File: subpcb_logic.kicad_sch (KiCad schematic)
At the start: 64 parts, among them J1 Conn_01x04, J12 xcore, J13 Screw_Terminal_01x02, J14 Conn_01x02, J15 Conn_01x04, J16 67800-8005, J18 67800-8005, J24 Conn_01x02, J25 67800-8005, J26 67800-8005, J27 67800-8005, J28 Conn_01x03_Male, J30 Conn_01x03_Male, J31 Conn_01x03_Pin, J52 Conn_01x03_Male, J54 Conn_01x03_Male, M1 Fan, Q1 AO3400A, Q2 AO3400A, U5 M24C02-WMN, U6 AS-RTK2B-MICRO-F9P-L1L2SMATH-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, U7 TXS0108EPW

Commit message: Added JLC part for xCore connector
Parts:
- J12: JLC (none) -> C306045
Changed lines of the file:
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@@
 			)
 		)
+		(property "JLC" "C306045"
+			(at 365.76 370.84 0)
+			(effects
+				(font
+					(size 1.27 1.27)
+				)
+				(hide yes)
+			)
+		)
 		(pin "114"
 		)
@@
 			)
 		)
+		(property "JLC" "C306045"
+			(at 201.93 424.18 0)
+			(effects
+				(font
+					(size 1.27 1.27)
+				)
+				(hide yes)
+			)
+		)
 		(pin "114"
 		)
@@
 			)
 		)
+		(property "JLC" "C306045"
+			(at 96.52 436.88 0)
+			(effects
+				(font
+					(size 1.27 1.27)
+				)
+				(hide yes)
+			)
+		)
 		(pin "114"
 		)
@@
 			)
 		)
+		(property "JLC" "C306045"
+			(at 97.79 345.44 0)
+			(effects
+				(font
+					(size 1.27 1.27)
+				)
+				(hide yes)
+			)
+		)
 		(pin "114"
 		)
@@
 			(at 364.49 425.45 0)
 			(effects
+				(font
+					(size 1.27 1.27)
+				)
+				(hide yes)
+			)
+		)
+		(property "JLC" "C306045"
+			(at 364.49 425.45 0)
+			(effects

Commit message: Updated to the non-pcb mount xt30 connectors
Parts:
- J14: footprint Connector_AMASS:AMASS_XT30UPB-M_1x02_P5.0mm_Vertical -> Connector_AMASS:AMASS_XT30U-M_1x02_P5.0mm_Vertical; JLC C428721 -> C99101
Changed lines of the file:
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@@
 			)
 		)
-		(property "Footprint" "Connector_AMASS:AMASS_XT30UPB-M_1x02_P5.0mm_Vertical"
+		(property "Footprint" "Connector_AMASS:AMASS_XT30U-M_1x02_P5.0mm_Vertical"
 			(at 54.61 218.44 0)
 			(effects
@@
 			)
 		)
-		(property "JLC" "C428721"
+		(property "JLC" "C99101"
 			(at 54.61 218.44 0)
 			(effects

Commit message: Added extension port, removed silkscreens
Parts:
- added J5: Conn_02x08_Odd_Even, Connector_PinHeader_2.54mm:PinHeader_2x08_P2.54mm_Vertical, symbol Connector_Generic:Conn_02x08_Odd_Even
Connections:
- net 3.3V: now also J5.3 (Pin_3), J5.4 (Pin_4)
- net 5V: now also J5.1 (Pin_1), J5.2 (Pin_2)
- net GND: now also J5.5 (Pin_5), J5.6 (Pin_6)
- net GPIO4: now reaches J12.137 (GPIO4)
- net GPIO4: now also J5.15 (Pin_15)
- net GPIO3: now reaches J12.139 (GPIO3)
- net GPIO3: now also J5.13 (Pin_13)
- net GPIO2: now reaches J12.141 (GPIO2)
- net GPIO2: now also J5.11 (Pin_11)
- net GPIO7: now reaches J12.143 (GPIO7)
- net GPIO7: now also J5.9 (Pin_9)
- net GPIO0: now reaches J12.145 (GPIO0)
- net GPIO0: now also J5.7 (Pin_7)
- net SPI2.MISO: now reaches J12.84 (SPI2.MISO)
- net SPI2.MISO: now also J5.12 (Pin_12)
- net SPI2.MOSI: now reaches J12.86 (SPI2.MOSI)
- net SPI2.MOSI: now also J5.14 (Pin_14)
- net SPI2.SCK: now reaches J12.88 (SPI2.SCK)
- net SPI2.SCK: now also J5.16 (Pin_16)
- net I2C2.SDA: now reaches J12.96 (I2C2.SDA)
- net I2C2.SDA: now also J5.8 (Pin_8)
- net I2C2.SCL: now reaches J12.98 (I2C2.SCL)
- net I2C2.SCL: now also J5.10 (Pin_10)
- no-connect marks 70 -> 60

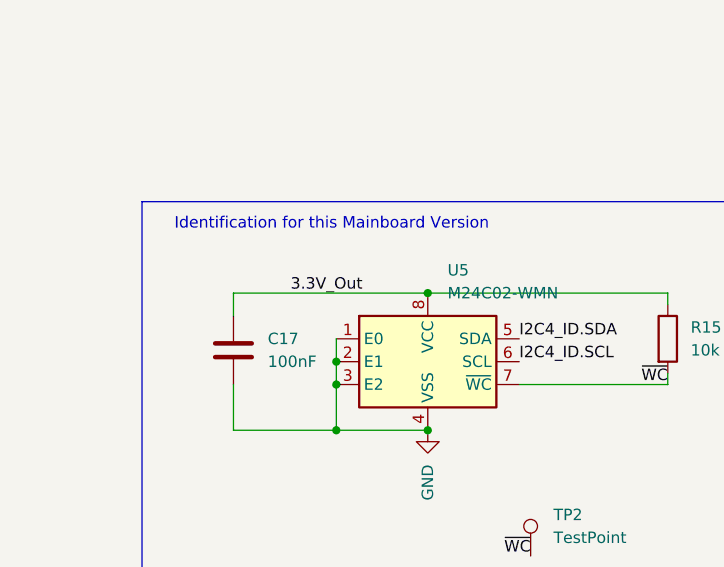
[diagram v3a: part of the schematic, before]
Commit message: Connected 3.3V for EEPROM
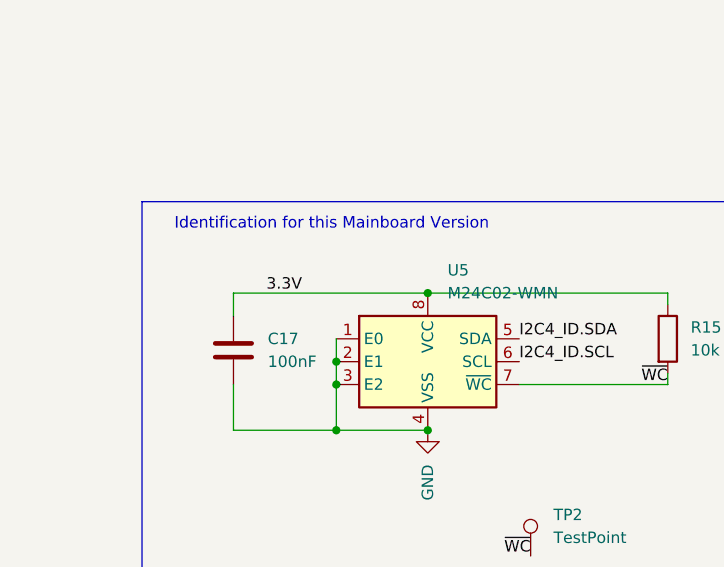
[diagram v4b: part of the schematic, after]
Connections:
- net 3.3V_Out is gone; now on net 3.3V: C17.1, R15.1, U5.8 (VCC)
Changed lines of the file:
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@@
-		)
-	)
-	(label "3.3V_Out"
-		(at 39.37 521.97 0)
-		(fields_autoplaced yes)
-		(effects
-			(font
-				(size 1.27 1.27)
-			)
-			(justify left bottom)
 		)
 	)
@@
 		)
 	)
+	(label "3.3V"
+		(at 40.64 521.97 180)
+		(fields_autoplaced yes)
+		(effects
+			(font
+				(size 1.27 1.27)
+			)
+			(justify right bottom)
+		)
+	)

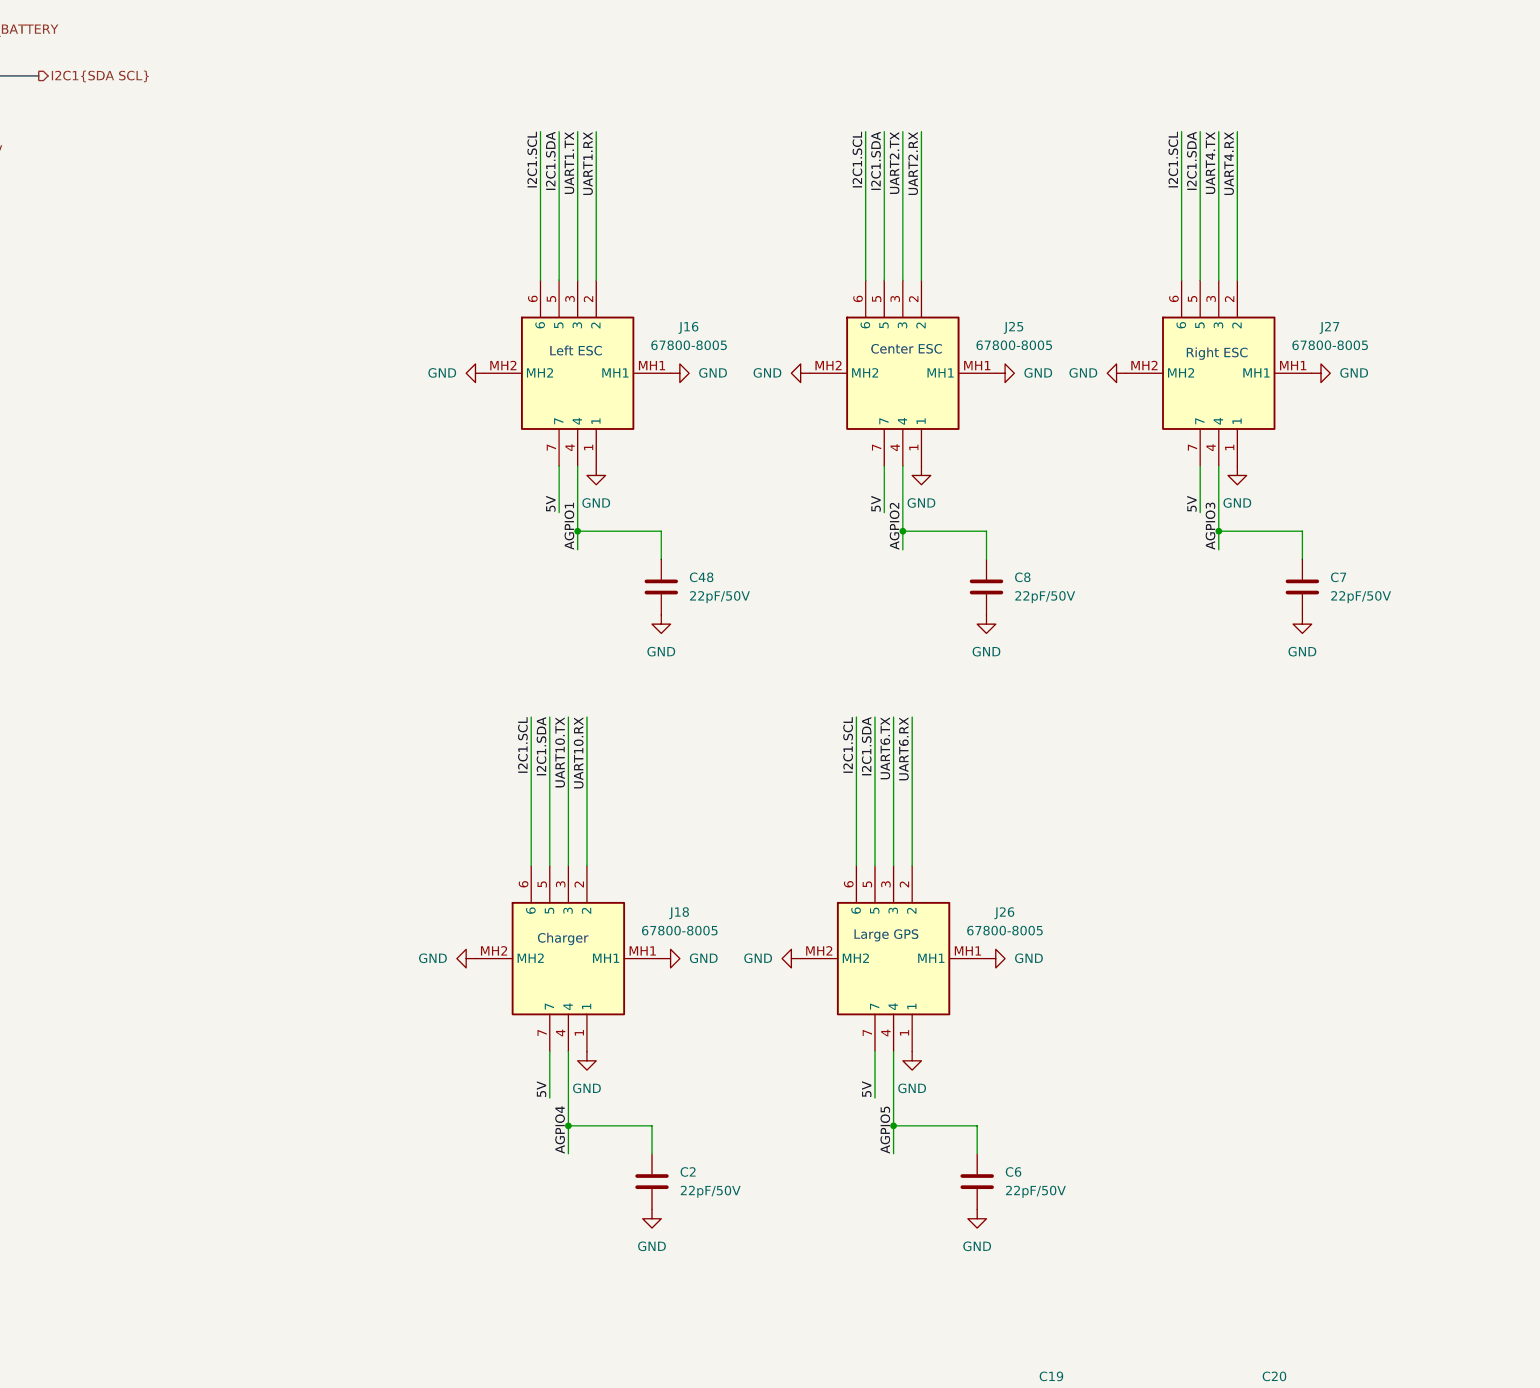
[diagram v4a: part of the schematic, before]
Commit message: Switched SATA to XH connectors
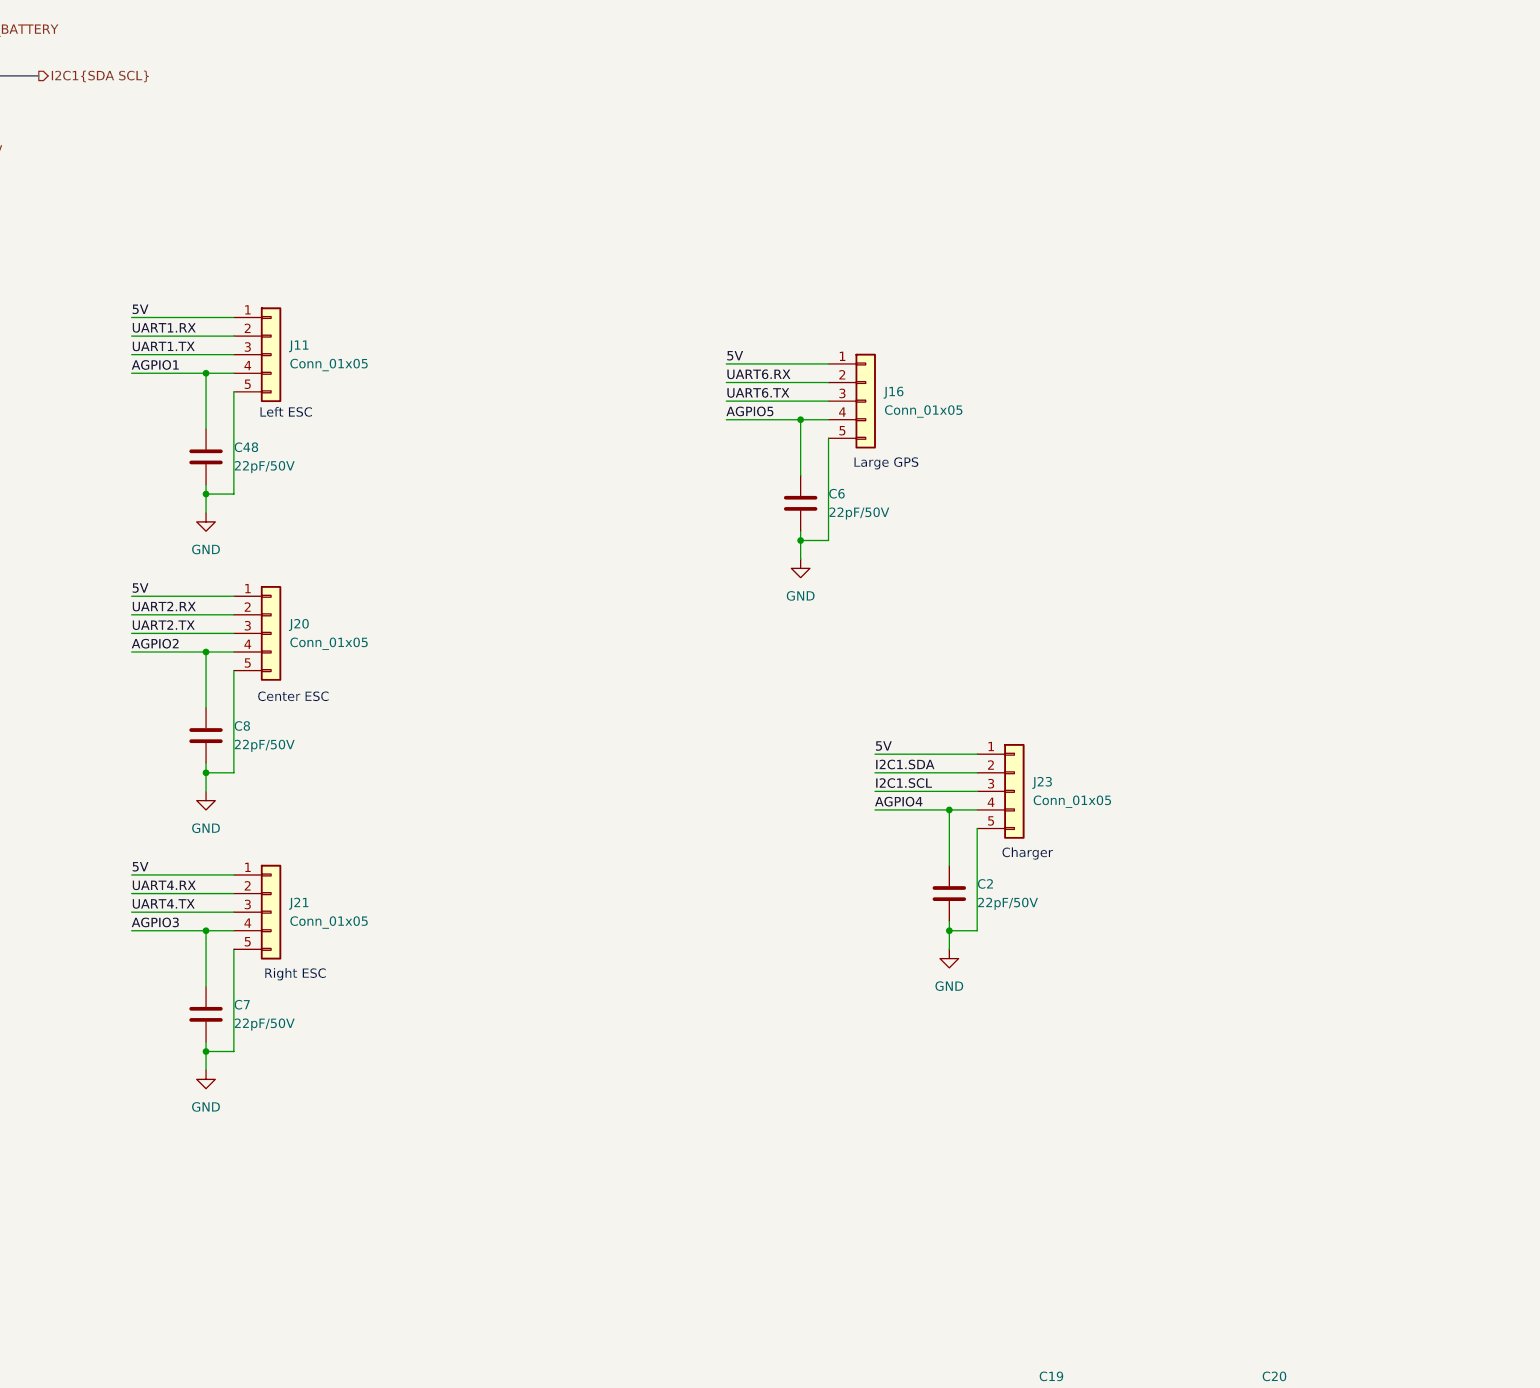
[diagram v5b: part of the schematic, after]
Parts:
- removed J16, J18, J25, J26, J27: 67800-8005, SATA-Molex-67800-8005:SATA-Molex-67800-8005, symbol SATA-Molex-67800-8005:67800-8005
- added J11, J16, J20, J21, J23: Conn_01x05, Connector_JST:JST_XH_B5B-XH-A_1x05_P2.50mm_Vertical, symbol Connector_Generic:Conn_01x05
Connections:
- net 5V: now also J11.1 (Pin_1), J16.1 (Pin_1), J20.1 (Pin_1), J21.1 (Pin_1), J23.1 (Pin_1)
- net AGPIO1: now also J11.4 (Pin_4)
- net AGPIO2: now also J20.4 (Pin_4)
- net AGPIO3: now also J21.4 (Pin_4)
- net AGPIO4: now also J23.4 (Pin_4)
- net AGPIO5: now also J16.4 (Pin_4)
- net GND: now also J11.5 (Pin_5), J16.5 (Pin_5), J20.5 (Pin_5), J21.5 (Pin_5), J23.5 (Pin_5)
- net I2C1.SCL: now also J23.3 (Pin_3)
- net I2C1.SDA: now also J23.2 (Pin_2)
- net UART1.RX: now also J11.2 (Pin_2)
- net UART1.TX: now also J11.3 (Pin_3)
- net UART2.RX: now also J20.2 (Pin_2)
- net UART2.TX: now also J20.3 (Pin_3)
- net UART4.RX: now also J21.2 (Pin_2)
- net UART4.TX: now also J21.3 (Pin_3)
- net UART6.RX: now also J16.2 (Pin_2)
- net UART6.TX: now also J16.3 (Pin_3)
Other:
- moved on the sheet: C2, C48, C6, C7, C8

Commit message: Fixed BOM
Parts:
- J11, J16, J20, J21, J23: JLC (none) -> C157991
- J28, J30, J52, J54: JLC C144394 -> C2937625

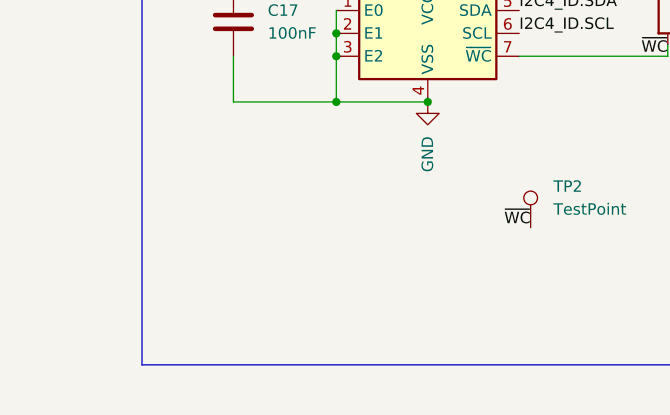
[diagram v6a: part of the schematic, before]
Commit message: Added I2C4 EEPROM Pins
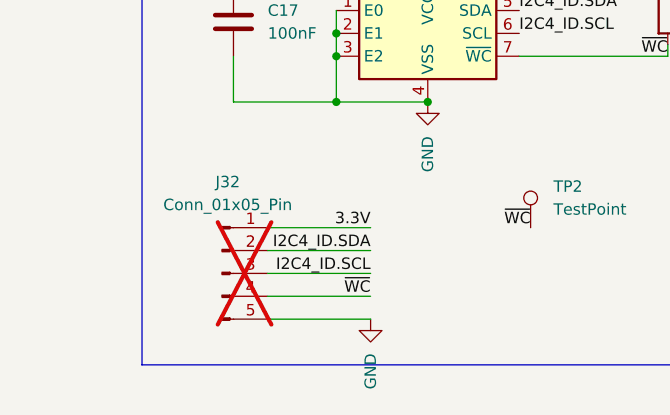
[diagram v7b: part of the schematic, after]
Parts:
- added J32: Conn_01x05_Pin, Connector_PinHeader_2.54mm:PinHeader_1x05_P2.54mm_Vertical, symbol Connector:Conn_01x05_Pin
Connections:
- net 3.3V: now also J32.1 (Pin_1)
- net GND: now also J32.5 (Pin_5)
- net I2C4_ID.SCL: now also J32.3 (Pin_3)
- net I2C4_ID.SDA: now also J32.2 (Pin_2)
- net ~{WC}: now also J32.4 (Pin_4)
